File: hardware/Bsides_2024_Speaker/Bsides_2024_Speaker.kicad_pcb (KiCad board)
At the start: 2 copper layers, 144.4 x 144.3 mm, 65 parts, among them J1 Add_On, J2 Battery, J3 Battery, J4 OLED, J5 Serial_IN, J6 Serial_OUT, P1 USB_C_Plug_USB2.0, Q1 DMG3415U-7, SW1 ON, SW2 SW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

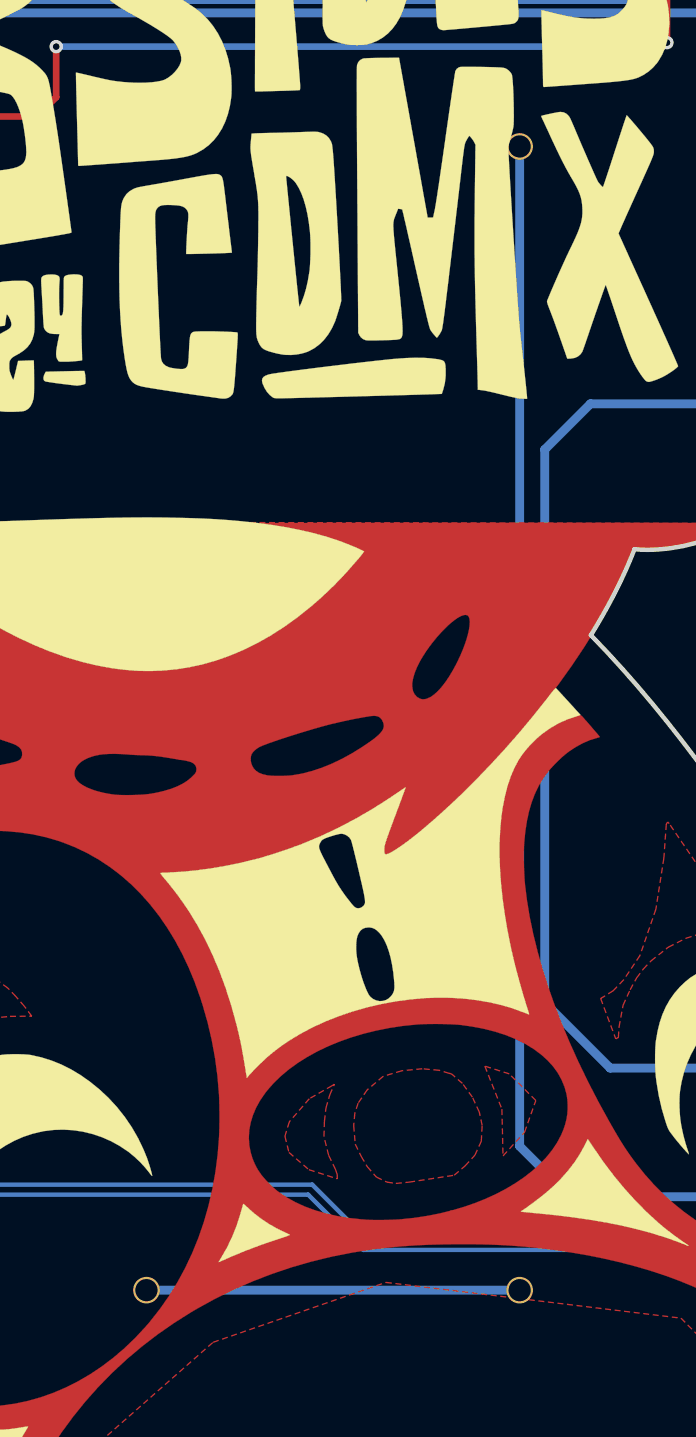
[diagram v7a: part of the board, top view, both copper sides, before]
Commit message: feat(Hw):Moved_Battery_Case
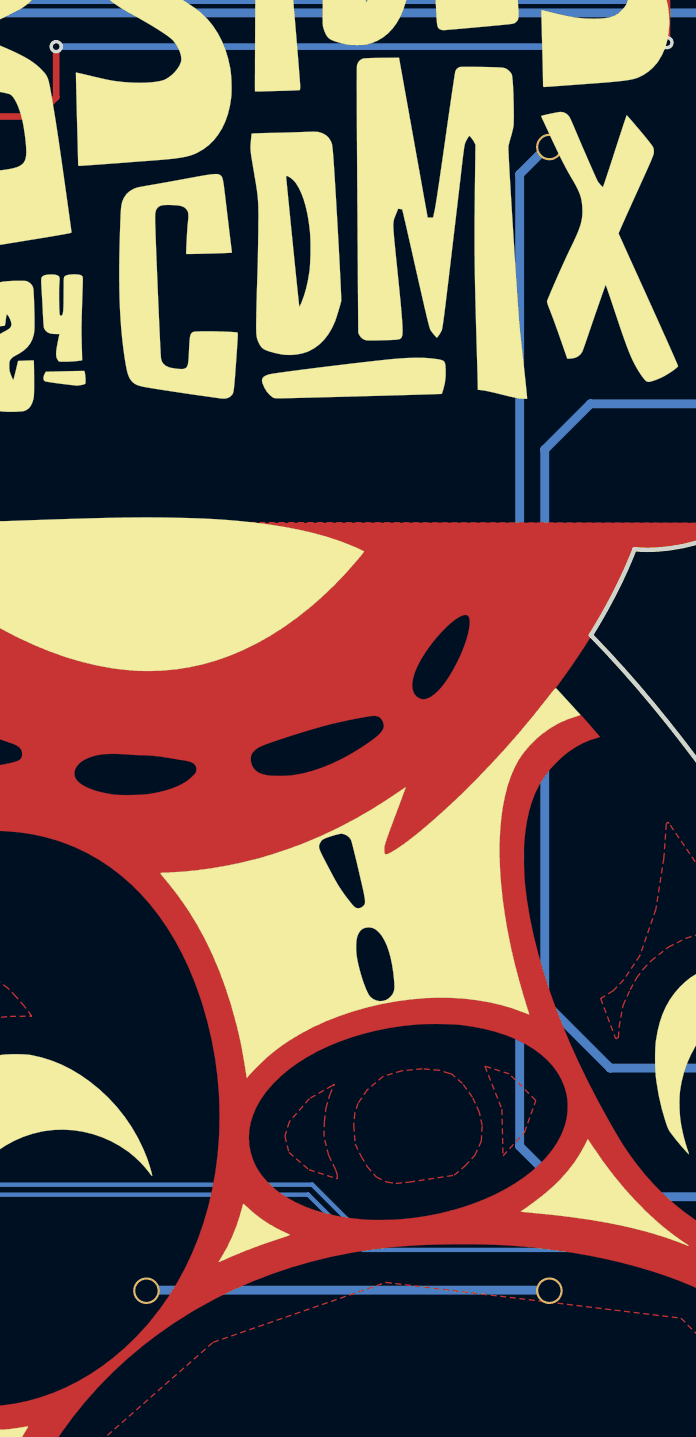
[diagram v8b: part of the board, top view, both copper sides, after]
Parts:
- moved J2 1.34 mm to (155.4, 76.9)
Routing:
- net Net-(J2-Pin_1): track 16.8 -> 18.2 mm
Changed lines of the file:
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@@
 	(footprint "bsides:BH-AA-A1AJ020"
 		(layer "B.Cu")
-		(at 137.288153 76.874107 90)
+		(at 137.288153 76.9 90)
 		(property "Reference" "J3"
 			(at 0 0.5 -90)
@@
 	(footprint "bsides:BH-AA-A1AJ020"
 		(layer "B.Cu")
-		(at 154.11 76.875 -90)
+		(at 155.45 76.9 -90)
 		(property "Reference" "J2"
 			(at 0 0.5 90)
@@
 	)
 	(segment
-		(start 154.11 51.1)
-		(end 154.11 96.16)
+		(start 155.45 51.015)
+		(end 154.11 52.355)
 		(width 0.4)
 		(layer "B.Cu")
@@
 	)
 	(segment
-		(start 153.903694 51.1)
-		(end 154.11 51.1)
-		(width 0.4)
-		(layer "B.Cu")
-		(net 20)
-	)
-	(segment
 		(start 185.56 96.92)
 		(end 198.235 96.92)
@@
 	)
 	(segment
-		(start 153.891847 51.111847)
-		(end 153.903694 51.1)
+		(start 154.11 52.355)
+		(end 154.11 96.16)
 		(width 0.4)
 		(layer "B.Cu")
@@
 	)
 	(segment
-		(start 154.109107 102.649107)
-		(end 154.11 102.65)
+		(start 137.288153 102.649107)
+		(end 155.365893 102.649107)
 		(width 0.4)
 		(layer "B.Cu")
@@
 	)
 	(segment
-		(start 137.288153 102.649107)
-		(end 154.109107 102.649107)
+		(start 155.365893 102.649107)
+		(end 155.45 102.565)
 		(width 0.4)
 		(layer "B.Cu")
